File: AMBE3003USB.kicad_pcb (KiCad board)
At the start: 2 copper layers, 95 x 85 mm, 209 parts, among them J1 McBSP, J2 USB_OTG, J4 CODEC, P1 GND, P2 Config, P3 3v3, P4 VSET, P5 HARD RESET, P6 SEQ, P7 3v3, P8 ACONF, P9 GND, Q1 BC847, U1 AMBE3003, U2 TPS75005RGW_wPin21, U3 FT232RL, X1 29.4912

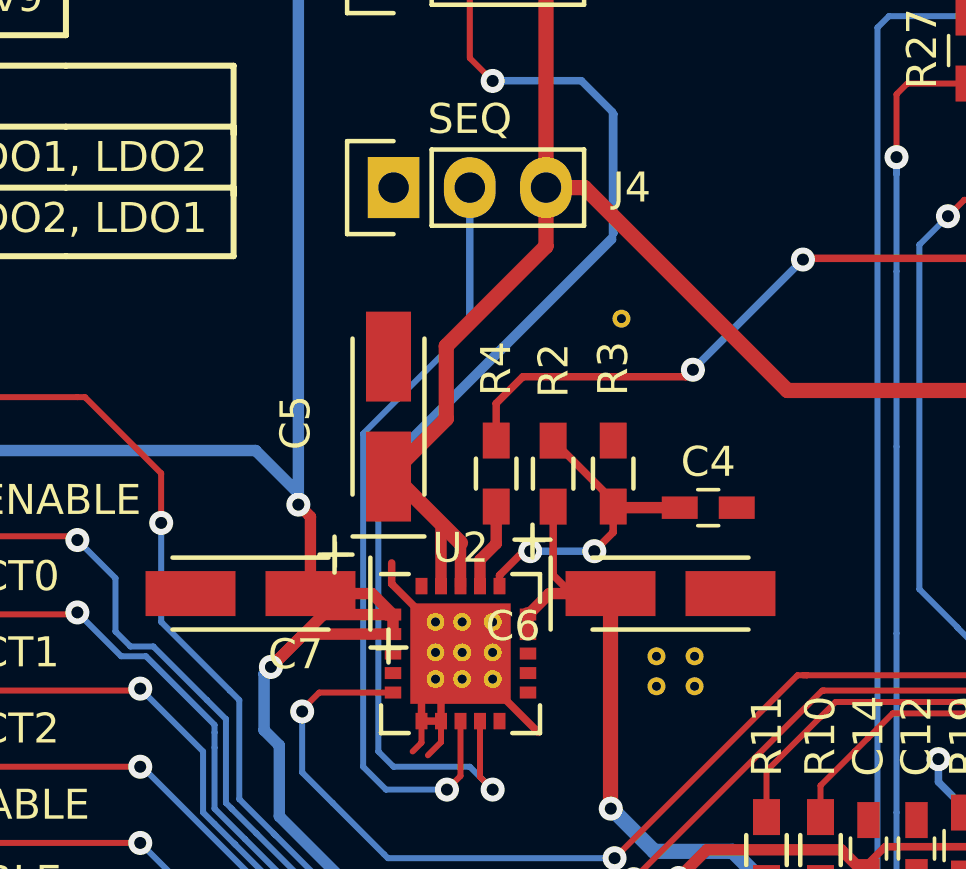
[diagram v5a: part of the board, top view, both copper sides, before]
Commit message: Add pull-up resistor for PWREN signal
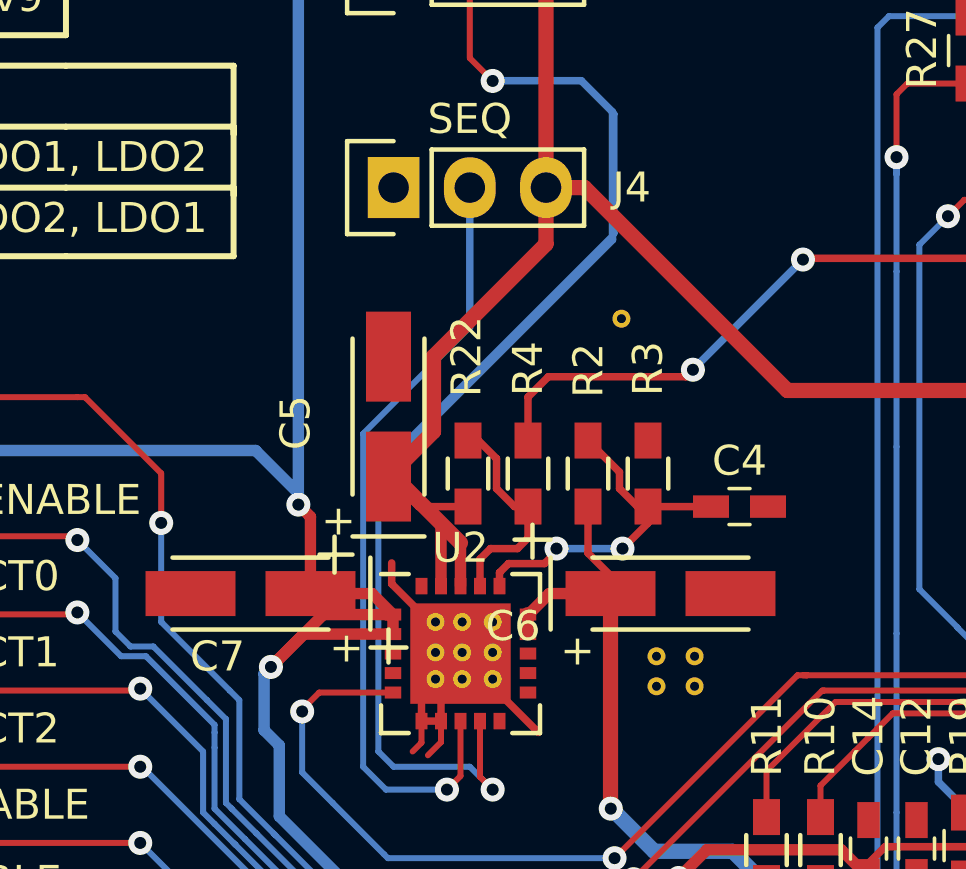
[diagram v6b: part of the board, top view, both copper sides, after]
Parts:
- added R22: 10k, Resistors_SMD:R_0603_HandSoldering, F.Cu at (67.2, 71.0)
- moved R2 1.16 mm to (71.2, 71.0)
- moved R3 1.16 mm to (73.2, 71.0)
- moved R4 1.06 mm to (69.2, 71.0)
- moved C4 1.04 mm to (76.3, 72.1)
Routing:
- net Net-(R22-Pad1): track 2.87 -> 7.34 mm
- net +5V: track 131.0 -> 134.1 mm
- net Net-(C4-Pad1): track 10.9 -> 12.0 mm
- net PWREN: track 22.6 -> 21.7 mm

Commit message: Bump version and date
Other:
- board text added: "v1.2 10/2017"
- board text removed: "v1.1 09/2017"
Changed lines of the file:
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@@
     (links 394)
     (no_connects 0)
-    (area 31.974499 47.974499 127.025501 133.025501)
+    (area 31.974499 41.5 138.65 133.025501)
     (thickness 1.6)
     (drawings 161)
@@
   )
   (setup
-    (last_trace_width 0.508)
+    (last_trace_width 0.25)
     (user_trace_width 0.2)
     (user_trace_width 0.254)
@@
     (effects (font (size 1 1) (thickness 0.15)) (justify left))
   )
-  (gr_text "v1.1\n09/2017" (at 103 53) (layer F.SilkS)
+  (gr_text "v1.2\n10/2017" (at 103 53) (layer F.SilkS)
     (effects (font (size 2 2) (thickness 0.5)) (justify left))
   )

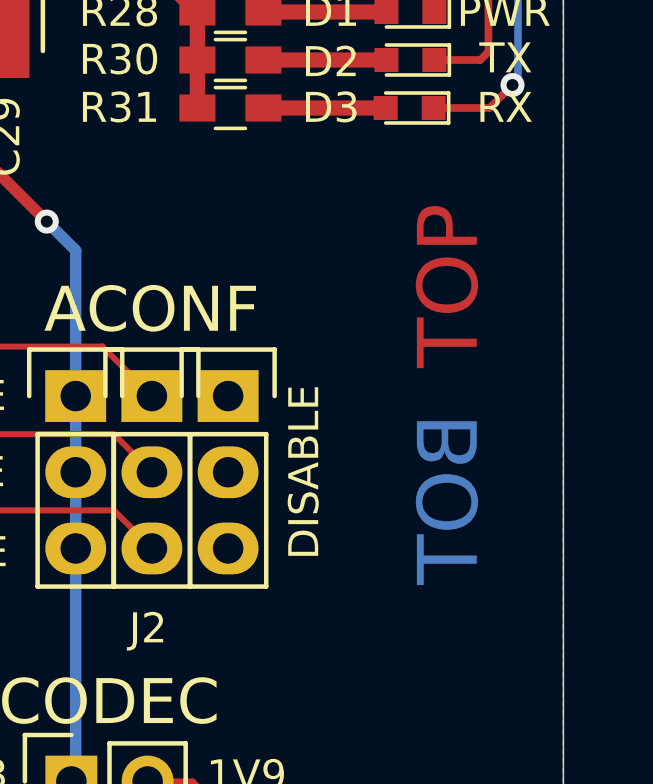
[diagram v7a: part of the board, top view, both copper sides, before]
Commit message: Add keepout area for top/bottom markers and add author info
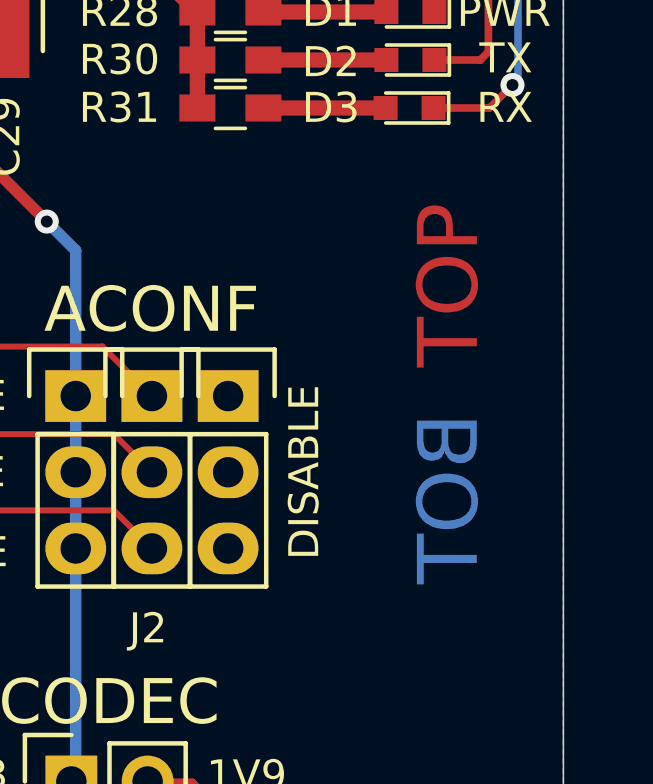
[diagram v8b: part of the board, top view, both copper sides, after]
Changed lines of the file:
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@@
   )
   (page A4)
+  (title_block
+    (title AMBE3003USB)
+    (date 2017-10-18)
+    (rev v1.2)
+    (company "DB9MAT & DF2ET")
+    (comment 1 mathis@giev.de)
+    (comment 2 df2et@df2et.de)
+    (comment 3 "CC-BY-NC-SA 3.0")
+  )
   (layers
     (0 F.Cu signal)
@@
     )
   )
+  (gr_text BOT (at 123.19 89.26 90) (layer B.Cu)
+    (effects (font (size 2 2) (thickness 0.5)) (justify mirror))
+  )
+  (gr_text TOP (at 123.19 82.15 90) (layer F.Cu)
+    (effects (font (size 2 2) (thickness 0.5)))
+  )
   (gr_text hardware (at 63.7286 122.7074) (layer F.SilkS)
     (effects (font (size 1.5 1.5) (thickness 0.3)))
@@
     (effects (font (size 1 1) (thickness 0.15)) (justify left))
   )
-  (gr_text BOT (at 123.19 89.281 90) (layer B.Cu)
-    (effects (font (size 2 2) (thickness 0.5)) (justify mirror))
-  )
-  (gr_text TOP (at 123.19 82.169 90) (layer F.Cu)
-    (effects (font (size 2 2) (thickness 0.5)))
-  )
   (gr_text RX (at 124.1 76.25) (layer F.SilkS)
     (effects (font (size 1 1) (thickness 0.15)) (justify left))
@@
       )
     )
+  )
+  (zone (net 0) (net_name "") (layer B.Cu) (hatch edge 0.508)
+    (connect_pads (clearance 0.508))
+    (min_thickness 0.254)
+    (keepout (tracks not_allowed) (vias not_allowed) (copperpour not_allowed))
+    (fill (arc_segments 16) (thermal_gap 0.508) (thermal_bridge_width 0.508))
+    (polygon
+      (pts
+        (xy 125.349 85.69198) (xy 120.53062 85.69198) (xy 120.53062 78.58252) (xy 125.349 78.58252) (xy 125.349 85.69198)
+      )
+    )
+  )
+  (zone (net 0) (net_name "") (layer F.Cu) (hatch edge 0.508)
+    (connect_pads (clearance 0.508))
+    (min_thickness 0.254)
+    (keepout (tracks not_allowed) (vias not_allowed) (copperpour not_allowed))
+    (fill (arc_segments 16) (thermal_gap 0.508) (thermal_bridge_width 0.508))
+    (polygon
+      (pts
+        (xy 125.349 92.82684) (xy 120.53062 92.82684) (xy 120.53062 85.71738) (xy 125.349 85.71738) (xy 125.349 92.82684)
+      )
+    )
